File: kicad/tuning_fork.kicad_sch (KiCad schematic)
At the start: 32 parts, among them J1 AudioIn, J2 TuningFork, J3 OscOut, J4 USB_B_Mini, J5 Conn_Coaxial, J6 Conn_Coaxial, J7 Iout, J8 AudioJack3, SW1 SW_SPDT, SW2 SW_SPDT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

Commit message: add RPi +5V supply header
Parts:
- added J9: Conn_01x03_Pin, Connector_PinSocket_2.54mm:PinSocket_1x03_P2.54mm_Vertical, symbol Connector:Conn_01x03_Pin
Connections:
- net GND: now also J9.3 (Pin_3)
- net VCC: now also J9.1 (Pin_1), J9.2 (Pin_2)

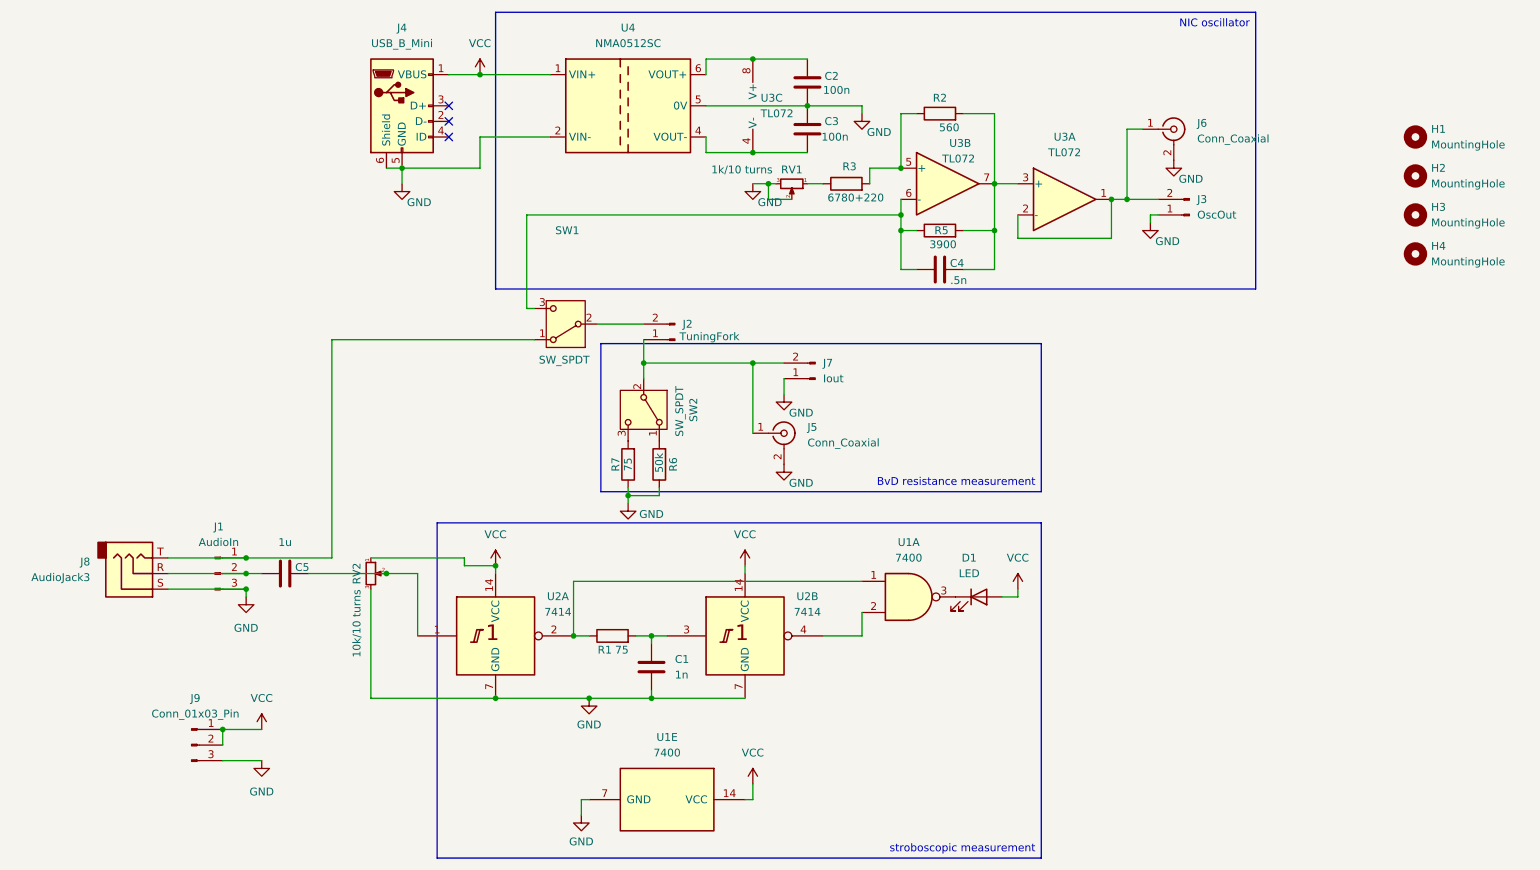
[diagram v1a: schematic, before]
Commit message: add oscillator reset push button
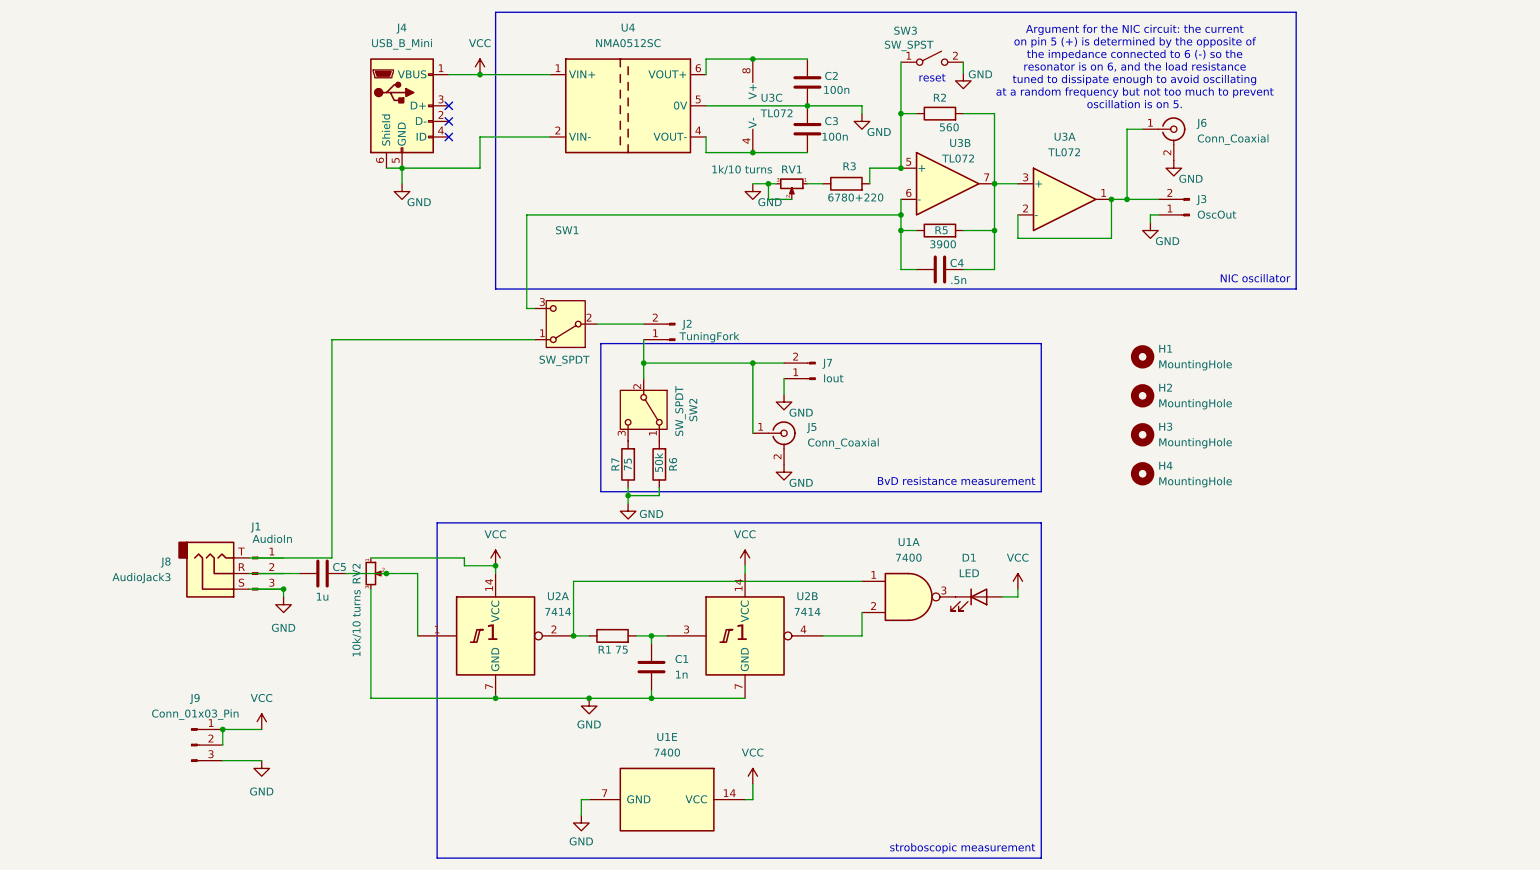
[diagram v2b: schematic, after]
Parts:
- added SW3: SW_SPST, Button_Switch_THT:SW_TH_Tactile_Omron_B3F-100x, symbol Switch:SW_SPST
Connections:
- net GND: now also SW3.2 (B)
- net at C5.1, J8.R: no longer J1.2 (Pin_2)
- net at J8.T, SW1.1 (A): no longer J1.1 (Pin_1)
- net at R2.1, R3.2, U3.5 (+): now also SW3.1 (A)
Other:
- note added: "Argument for the NIC circuit: the current on pin 5 (+) is determined by the opposite of the impedance connected to 6 (-) so the resonator is on 6, and the load resistance tuned to dissipate enough to avoid oscillating at a random frequency but not too much to prevent oscillation is on 5."
- note added: "reset"
- moved on the sheet: C5, H1, H2, H3, H4, J1, J8
